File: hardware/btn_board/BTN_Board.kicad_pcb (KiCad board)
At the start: 2 copper layers, 125 x 25 mm, 14 parts, among them J2 Conn_01x10, SW1 SW_Push_Dual_x2, SW2 SW_Push_Dual_x2, SW3 SW_Push_Dual_x2, SW4 SW_Push_Dual_x2, SW5 SW_Push_Dual_x2

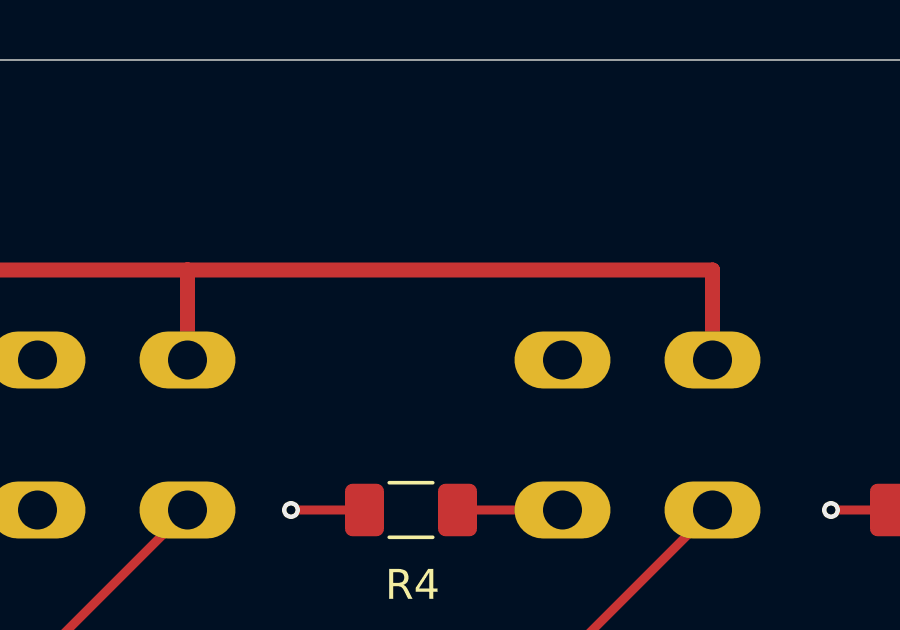
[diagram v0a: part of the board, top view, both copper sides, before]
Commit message: Finished btn board and generated gerbers
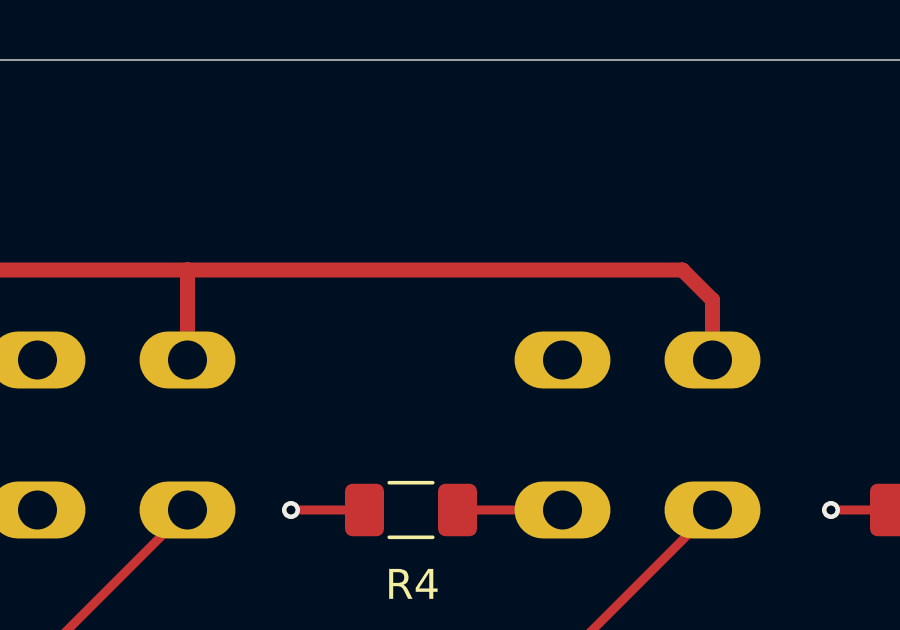
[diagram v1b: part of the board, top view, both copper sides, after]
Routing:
- net /5V_In: track 88.4 -> 87.8 mm
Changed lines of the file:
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@@
 			(outputformat 1)
 			(mirror no)
-			(drillshape 1)
+			(drillshape 0)
 			(scaleselection 1)
-			(outputdirectory "")
+			(outputdirectory "C:/Users/gglas/repos/swim_clock_general/hardware/btn_board/")
 		)
 	)
@@
 	)
 	(segment
+		(start 101.5 63.5)
+		(end 93.75 55.75)
+		(width 0.3)
+		(layer "F.Cu")
+		(net 6)
+	)
+	(segment
+		(start 158.5 57.5)
+		(end 152.5 63.5)
+		(width 0.3)
+		(layer "F.Cu")
+		(net 6)
+	)
+	(segment
+		(start 167.5 57.5)
+		(end 171 57.5)
+		(width 0.3)
+		(layer "F.Cu")
+		(net 6)
+	)
+	(segment
+		(start 152.5 63.5)
+		(end 101.5 63.5)
+		(width 0.3)
+		(layer "F.Cu")
+		(net 6)
+	)
+	(segment
 		(start 93.75 55.75)
 		(end 91 55.75)
@@
 	)
 	(segment
-		(start 167.5 57.5)
-		(end 171 57.5)
-		(width 0.3)
-		(layer "F.Cu")
-		(net 6)
-	)
-	(segment
-		(start 158.5 57.5)
-		(end 152.5 63.5)
-		(width 0.3)
-		(layer "F.Cu")
-		(net 6)
-	)
-	(segment
-		(start 101.5 63.5)
-		(end 93.75 55.75)
-		(width 0.3)
-		(layer "F.Cu")
-		(net 6)
-	)
-	(segment
-		(start 152.5 63.5)
-		(end 101.5 63.5)
-		(width 0.3)
-		(layer "F.Cu")
-		(net 6)
-	)
-	(segment
 		(start 100 49.5)
 		(end 123.5 49.5)
@@
 	)
 	(segment
-		(start 141 49.5)
-		(end 158.5 49.5)
+		(start 158.5 50.5)
+		(end 158.5 52.5)
 		(width 0.5)
 		(layer "F.Cu")
@@
 	)
 	(segment
+		(start 141 49.5)
+		(end 157.5 49.5)
+		(width 0.5)
+		(layer "F.Cu")
+		(net 8)
+	)
+	(segment
 		(start 84.5 50.5)
 		(end 84.5 52.5)
@@
 	)
 	(segment
+		(start 157.5 49.5)
+		(end 158.5 50.5)
+		(width 0.5)
+		(layer "F.Cu")
+		(net 8)
+	)
+	(segment
 		(start 85.5 49.5)
 		(end 93 49.5)
 		(width 0.5)
 		(layer "F.Cu")
-		(net 8)
-	)
-	(segment
-		(start 158.5 49.5)
-		(end 158.5 52.5)
-		(width 0.5)
-		(layer "F.Cu")
